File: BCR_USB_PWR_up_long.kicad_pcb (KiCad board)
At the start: 2 copper layers, 13.4 x 21.8 mm, 2 parts, among them CN1 DB9_Female, CN2 UE27AC54100

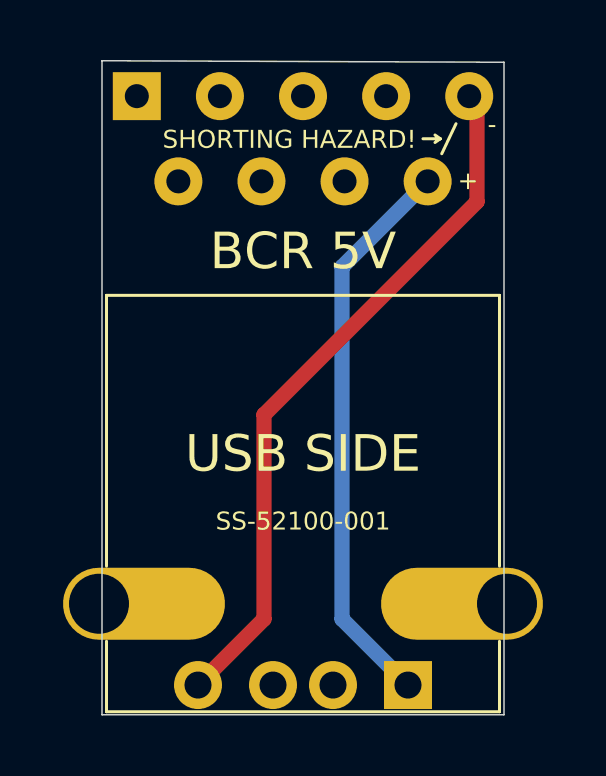
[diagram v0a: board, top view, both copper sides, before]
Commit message: rename NEC to up_long, and a short up version that covers up the shorting hazard
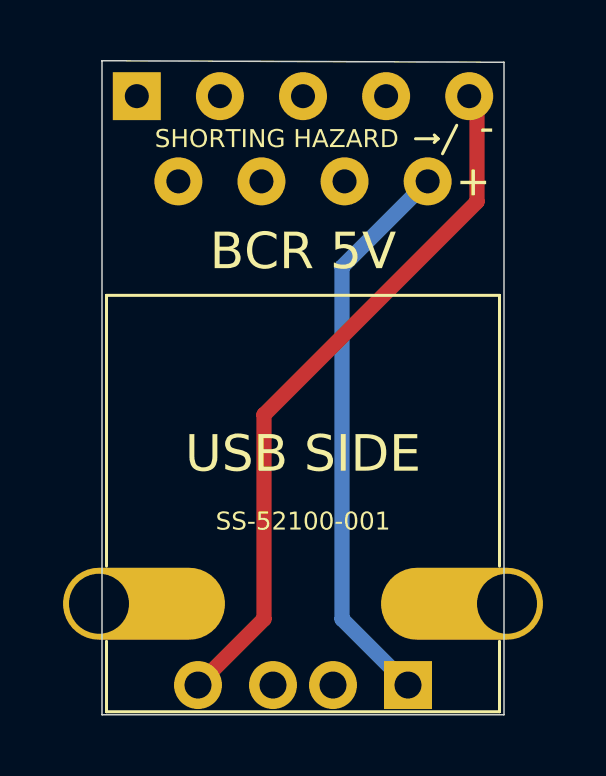
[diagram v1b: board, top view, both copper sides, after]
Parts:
- CN1: footprint 0_LOCAL:TE-5207826_nec -> 0_LOCAL:A-DF_09_PP-Z_nec
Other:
- board text added: "A-DF 09 PP/Z"
- board text added: "SHORTING HAZARD"
- board text removed: "NEC PC-8201 / PC-8300"
- board text removed: "SHORTING HAZARD!"
- board text removed: "TE 5207826"
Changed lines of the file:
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@@
   (general
     (thickness 1.6)
-    (drawings 24)
+    (drawings 23)
     (tracks 8)
     (zones 0)
@@
     (add_net "Net-(CN2-PadSH)")
   )
-  (module 0_LOCAL:TE-5207826_nec (layer B.Cu)
+  (module 0_LOCAL:A-DF_09_PP-Z_nec (layer B.Cu)
     (at 121.46026 94.33814 180)
     (descr "9-pin D-Sub connector, straight/vertical, THT-mount, female, pitch 2.77x2.84mm, distance of mounting holes 25mm, see https://disti-assets.s3.amazonaws.com/tonar/files/datasheets/16730.pdf")
@@
     (pad 2 thru_hole circle (at -2.77 0 180) (size 1.6 1.6) (drill 0.8) (layers *.Cu *.Mask))
     (pad 1 thru_hole rect (at 0 0 180) (size 1.6 1.6) (drill 0.8) (layers *.Cu *.Mask))
-    (model ${KIPRJMOD}/3dmodels/TE-5207826_short_legs.step
-      (offset (xyz -5.528 -1.42 11.4))
+    (model ${KIPRJMOD}/3dmodels/DE9F_metal.step
+      (offset (xyz -5.54 -1.42 6.3))
       (scale (xyz 1 1 1))
       (rotate (xyz 0 0 0))
@@
     )
   )
-  (gr_line (start 131.575 95.758) (end 131.4 95.883) (layer F.SilkS) (width 0.1016))
-  (gr_line (start 131.575 95.758) (end 131.4 95.633) (layer F.SilkS) (width 0.1016))
-  (gr_line (start 131.575 95.758) (end 131 95.758) (layer F.SilkS) (width 0.1016))
-  (gr_text + (at 132.5 97.158) (layer F.SilkS)
+  (gr_line (start 131.5 95.758) (end 131.375 95.633) (layer F.SilkS) (width 0.1016))
+  (gr_line (start 131.5 95.758) (end 131.375 95.883) (layer F.SilkS) (width 0.1016))
+  (gr_line (start 131.5 95.758) (end 130.75 95.758) (layer F.SilkS) (width 0.1016))
+  (gr_line (start 131.65 96.258) (end 132.125 95.308) (layer F.SilkS) (width 0.1016))
+  (gr_text "SHORTING HAZARD" (at 126.125 95.758) (layer F.SilkS)
     (effects (font (size 0.6 0.6) (thickness 0.06)))
   )
-  (gr_text - (at 133.3 95.283) (layer F.SilkS)
-    (effects (font (size 0.6 0.6) (thickness 0.06)))
-  )
-  (gr_line (start 132.1 95.258) (end 131.625 96.258) (layer F.SilkS) (width 0.1016))
-  (gr_text "SHORTING HAZARD!" (at 126.55 95.783) (layer F.SilkS)
-    (effects (font (size 0.6 0.6) (thickness 0.06)))
-  )
-  (gr_text "from BCR port" (at 126.9 104.658) (layer B.SilkS)
+  (gr_text - (at 133.125 95.383) (layer F.SilkS)
+    (effects (font (size 1 1) (thickness 0.1)))
+  )
+  (gr_text + (at 132.675 97.183) (layer F.SilkS)
+    (effects (font (size 1 1) (thickness 0.1)))
+  )
+  (gr_text "A-DF 09 PP/Z" (at 127 95.758) (layer B.SilkS)
+    (effects (font (size 0.6 0.6) (thickness 0.1)) (justify mirror))
+  )
+  (gr_text "from BCR port" (at 127 107.333) (layer B.SilkS)
     (effects (font (size 1 1) (thickness 0.1)) (justify mirror))
   )
@@
     (effects (font (size 0.6 0.6) (thickness 0.1)))
   )
-  (gr_text "TE 5207826" (at 127 95.758) (layer B.SilkS)
-    (effects (font (size 0.6 0.6) (thickness 0.1)) (justify mirror))
-  )
   (gr_text github.com/bkw777/BCR_USB_PWR (at 127.1 109.258) (layer B.SilkS)
     (effects (font (size 0.5 0.5) (thickness 0.1)) (justify mirror))
   )
-  (gr_text "NEC PC-8201 / PC-8300" (at 127 106.858) (layer B.SilkS)
-    (effects (font (size 0.6 0.6) (thickness 0.1)) (justify mirror))
-  )
-  (gr_text "5v USB power" (at 127 102.958) (layer B.SilkS)
+  (gr_text "5v USB power" (at 127 105.508) (layer B.SilkS)
     (effects (font (size 1 1) (thickness 0.1)) (justify mirror))
   )

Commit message: Add BCR_Breakout. Rename repo to BCR_Breakout.
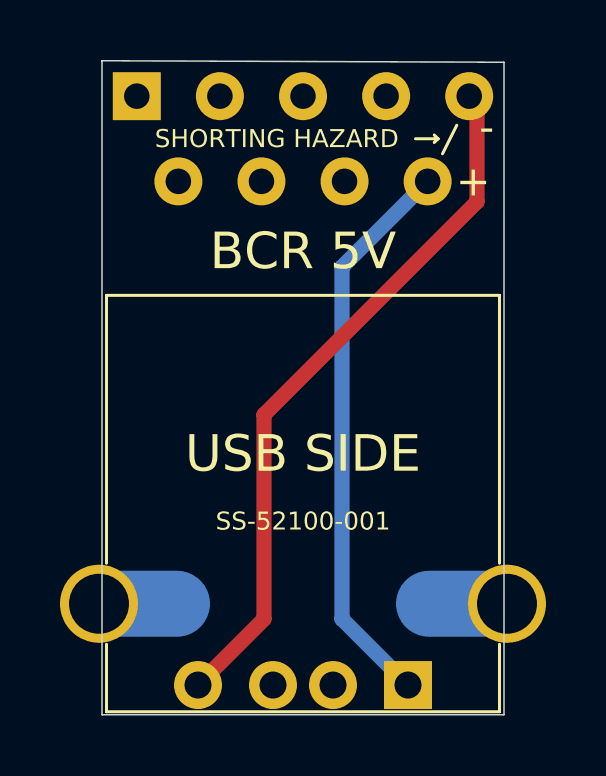
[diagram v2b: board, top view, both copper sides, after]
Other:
- board text added: "github.com/bkw777/BCR_Breakout"
- board text removed: "github.com/bkw777/BCR_USB_PWR"
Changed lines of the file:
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@@
     (fp_line (start -21.04 -6.74) (end 9.96 -6.74) (layer B.CrtYd) (width 0.05))
     (fp_line (start -21.04 3.91) (end -21.04 -6.74) (layer B.CrtYd) (width 0.05))
-    (fp_line (start -10.942952 -5.43) (end -0.137048 -5.43) (layer B.SilkS) (width 0.12))
     (fp_line (start -13.358887 0.652163) (end -12.53015 -4.047837) (layer B.Fab) (width 0.1))
     (fp_line (start 2.278887 0.652163) (end 1.45015 -4.047837) (layer B.Fab) (width 0.1))
     (fp_line (start -10.954457 -5.37) (end -0.125543 -5.37) (layer B.Fab) (width 0.1))
     (fp_line (start -11.783194 2.53) (end 0.703194 2.53) (layer B.Fab) (width 0.1))
-    (fp_arc (start -0.137048 -3.77) (end -0.137048 -5.43) (angle 52.39100523) (layer B.SilkS) (width 0.12))
-    (fp_arc (start -10.942952 -3.77) (end -10.942952 -5.43) (angle -52.80148662) (layer B.SilkS) (width 0.12))
     (fp_arc (start -0.125543 -3.77) (end -0.125543 -5.37) (angle 80) (layer B.Fab) (width 0.1))
     (fp_arc (start -10.954457 -3.77) (end -10.954457 -5.37) (angle -80) (layer B.Fab) (width 0.1))
@@
     (fp_line (start -5.54 -0.82) (end -5.54 -2.02) (layer Dwgs.User) (width 0.01))
     (fp_line (start -6.54 -1.42) (end -4.54 -1.42) (layer Dwgs.User) (width 0.01))
-    (pad 9 thru_hole circle (at -9.695 -2.84 180) (size 1.6 1.6) (drill 0.8) (layers *.Cu *.Mask)
+    (pad 9 thru_hole circle (at -9.695 -2.84 180) (size 1.6 1.6) (drill 0.85) (layers *.Cu *.Mask)
       (net 1 /+5V))
-    (pad 8 thru_hole circle (at -6.925 -2.84 180) (size 1.6 1.6) (drill 0.8) (layers *.Cu *.Mask))
-    (pad 7 thru_hole circle (at -4.155 -2.84 180) (size 1.6 1.6) (drill 0.8) (layers *.Cu *.Mask))
-    (pad 6 thru_hole circle (at -1.385 -2.84 180) (size 1.6 1.6) (drill 0.8) (layers *.Cu *.Mask))
-    (pad 5 thru_hole circle (at -11.08 0 180) (size 1.6 1.6) (drill 0.8) (layers *.Cu *.Mask)
+    (pad 8 thru_hole circle (at -6.925 -2.84 180) (size 1.6 1.6) (drill 0.85) (layers *.Cu *.Mask))
+    (pad 7 thru_hole circle (at -4.155 -2.84 180) (size 1.6 1.6) (drill 0.85) (layers *.Cu *.Mask))
+    (pad 6 thru_hole circle (at -1.385 -2.84 180) (size 1.6 1.6) (drill 0.85) (layers *.Cu *.Mask))
+    (pad 5 thru_hole circle (at -11.08 0 180) (size 1.6 1.6) (drill 0.85) (layers *.Cu *.Mask)
       (net 2 /GND))
-    (pad 4 thru_hole circle (at -8.31 0 180) (size 1.6 1.6) (drill 0.8) (layers *.Cu *.Mask))
-    (pad 3 thru_hole circle (at -5.54 0 180) (size 1.6 1.6) (drill 0.8) (layers *.Cu *.Mask))
-    (pad 2 thru_hole circle (at -2.77 0 180) (size 1.6 1.6) (drill 0.8) (layers *.Cu *.Mask))
-    (pad 1 thru_hole rect (at 0 0 180) (size 1.6 1.6) (drill 0.8) (layers *.Cu *.Mask))
+    (pad 4 thru_hole circle (at -8.31 0 180) (size 1.6 1.6) (drill 0.85) (layers *.Cu *.Mask))
+    (pad 3 thru_hole circle (at -5.54 0 180) (size 1.6 1.6) (drill 0.85) (layers *.Cu *.Mask))
+    (pad 2 thru_hole circle (at -2.77 0 180) (size 1.6 1.6) (drill 0.85) (layers *.Cu *.Mask))
+    (pad 1 thru_hole rect (at 0 0 180) (size 1.6 1.6) (drill 0.85) (layers *.Cu *.Mask))
     (model ${KIPRJMOD}/3dmodels/DE9F_metal.step
       (offset (xyz -5.54 -1.42 6.3))
@@
     )
     (fp_line (start -6.55 -3.6) (end 6.55 -3.6) (layer F.SilkS) (width 0.1))
-    (fp_line (start 6.55 1.25) (end 6.55 10.28) (layer F.SilkS) (width 0.1))
-    (fp_line (start -6.55 1.25) (end -6.55 10.28) (layer F.SilkS) (width 0.1))
-    (fp_line (start -6.55 -3.6) (end -6.55 -1.25) (layer F.SilkS) (width 0.1))
+    (fp_line (start 6.55 1.35) (end 6.55 10.28) (layer F.SilkS) (width 0.1))
+    (fp_line (start -6.55 1.35) (end -6.55 10.28) (layer F.SilkS) (width 0.1))
+    (fp_line (start -6.55 -3.6) (end -6.55 -1.35) (layer F.SilkS) (width 0.1))
     (fp_line (start -6.55 -3.6) (end 6.55 -3.6) (layer F.Fab) (width 0.1))
     (fp_line (start 6.55 -3.6) (end 6.55 10.28) (layer F.Fab) (width 0.1))
     (fp_line (start -6.55 -3.6) (end -6.55 10.28) (layer F.Fab) (width 0.1))
     (fp_line (start -6.55 10.28) (end 6.55 10.28) (layer F.Fab) (width 0.1))
-    (fp_line (start 6.55 -3.6) (end 6.55 -1.25) (layer F.SilkS) (width 0.1))
+    (fp_line (start 6.55 -3.6) (end 6.55 -1.35) (layer F.SilkS) (width 0.1))
     (fp_line (start 6.55 10.28) (end -6.55 10.28) (layer F.SilkS) (width 0.1))
     (fp_line (start -6.75 -3.94) (end 6.75 -3.94) (layer F.CrtYd) (width 0.05))
@@
       (effects (font (size 1 1) (thickness 0.15)))
     )
+    (pad SH smd oval (at 7 0 180) (size 4.8 2.2) (drill (offset -1.5 0)) (layers B.Cu B.Paste B.Mask)
+      (net 3 "Net-(CN2-PadSH)"))
+    (pad SH smd oval (at -7 0 180) (size 4.8 2.2) (drill (offset 1.5 0)) (layers B.Cu B.Paste B.Mask)
+      (net 3 "Net-(CN2-PadSH)"))
     (pad 4 thru_hole circle (at 3.5 -2.71 180) (size 1.6 1.6) (drill 0.9) (layers *.Cu *.Mask)
       (net 2 /GND))
@@
     (pad 1 thru_hole rect (at -3.5 -2.71 180) (size 1.6 1.6) (drill 0.9) (layers *.Cu *.Mask)
       (net 1 /+5V))
-    (pad SH thru_hole oval (at 6.8 0 180) (size 5.4 2.4) (drill 2 (offset -1.5 0)) (layers *.Cu *.Mask)
+    (pad SH thru_hole circle (at 6.8 0 180) (size 2.6 2.6) (drill 2) (layers *.Cu *.Mask)
       (net 3 "Net-(CN2-PadSH)"))
-    (pad SH thru_hole oval (at -6.8 0 180) (size 5.4 2.4) (drill 2 (offset 1.5 0)) (layers *.Cu *.Mask)
+    (pad SH thru_hole circle (at -6.8 0 180) (size 2.6 2.6) (drill 2) (layers *.Cu *.Mask)
       (net 3 "Net-(CN2-PadSH)"))
     (model ${KIPRJMOD}/3dmodels/USB-A_female_horiz_thru.step
@@
     (effects (font (size 0.6 0.6) (thickness 0.1)))
   )
-  (gr_text github.com/bkw777/BCR_USB_PWR (at 127.1 109.258) (layer B.SilkS)
+  (gr_text github.com/bkw777/BCR_Breakout (at 127.1 109.258) (layer B.SilkS)
     (effects (font (size 0.5 0.5) (thickness 0.1)) (justify mirror))
   )
